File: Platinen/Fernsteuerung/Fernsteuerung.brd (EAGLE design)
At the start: 98 x 90 mm, 3 parts, among them K1 ESP32DEVKITV11000MIL, P1 TFT_3.5"_SPI_480X320, U1 COM-09032

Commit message: Eagle Fernsteuerung
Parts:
- added G1: BATT3V3_AA, HTL22_basis:BATT-3V3-AA
- moved K1 18.3 mm to (61.4, 35.2), turned to 90 degrees
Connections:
- net +3V3: now also G1.PLUS
- net GND: now also G1.MINUS, U1.B2B; no longer U1.B2A
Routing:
- net TFT_MISO: track 0.00 -> 147.3 mm
- net +3V3: track 0.00 -> 119.6 mm, vias 0 -> 2
- net TFT_CS: track 0.00 -> 91.2 mm
- net TFT_SCK: track 0.00 -> 88.2 mm
- net TFT_DC: track 0.00 -> 63.6 mm
- net TFT_RESET: track 0.00 -> 63.6 mm
- net JOYSTICK_X: track 0.00 -> 59.6 mm
- net JOYSTICK_SELECT: track 0.00 -> 27.7 mm
- net JOYSTICK_Y: track 0.00 -> 25.9 mm
- added copper zone on layer 16, net GND
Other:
- board text added: "David Kedra Diplomarbeit Fernsteuerung"

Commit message: board fersteuerung
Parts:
- added R1: 10k, HTL22_basis:R1206
- added S1: TASTERB3F-1000, HTL22_basis:B3F-10XX
- added S2: SCHALTER1SX254, HTL22_basis:SX254
- moved K1 50.4 mm to (82.1, 81.0), turned to 270 degrees
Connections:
- new net N$1: K1.4, R1.2, S1.3
- new net N$2: G1.PLUS, S2.W1
- net +3V3: now also S1.1, S2.O1; no longer G1.PLUS
- net GND: now also R1.1
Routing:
- net TFT_MISO: track 147.3 -> 0.00 mm
- net +3V3: track 119.6 -> 0.00 mm, vias 2 -> 0
- net TFT_CS: track 91.2 -> 0.00 mm
- net TFT_SCK: track 88.2 -> 0.00 mm
- net TFT_DC: track 63.6 -> 0.00 mm
- net TFT_RESET: track 63.6 -> 0.00 mm
- net JOYSTICK_X: track 59.6 -> 0.00 mm
- net JOYSTICK_SELECT: track 27.7 -> 0.00 mm
- net JOYSTICK_Y: track 25.9 -> 0.00 mm

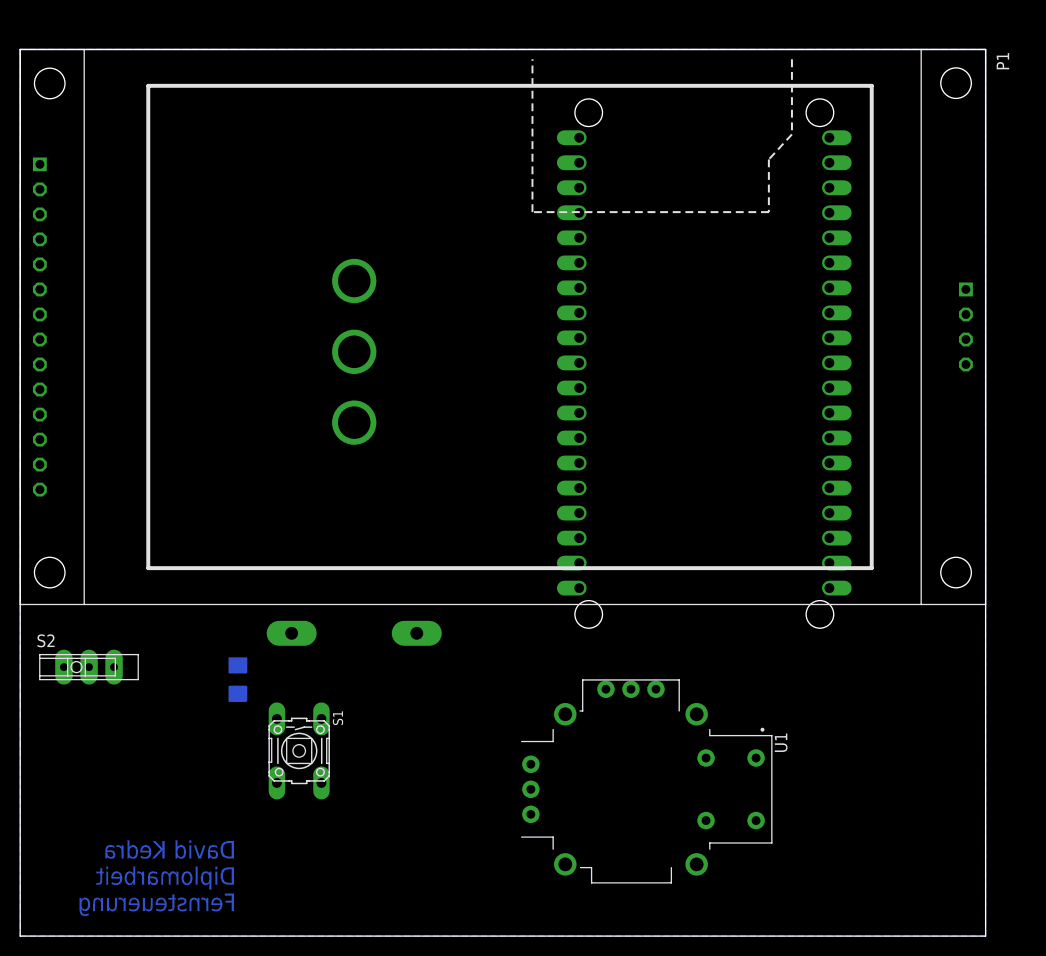
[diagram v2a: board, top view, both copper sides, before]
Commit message: Fernsteuerung Plaine fertig
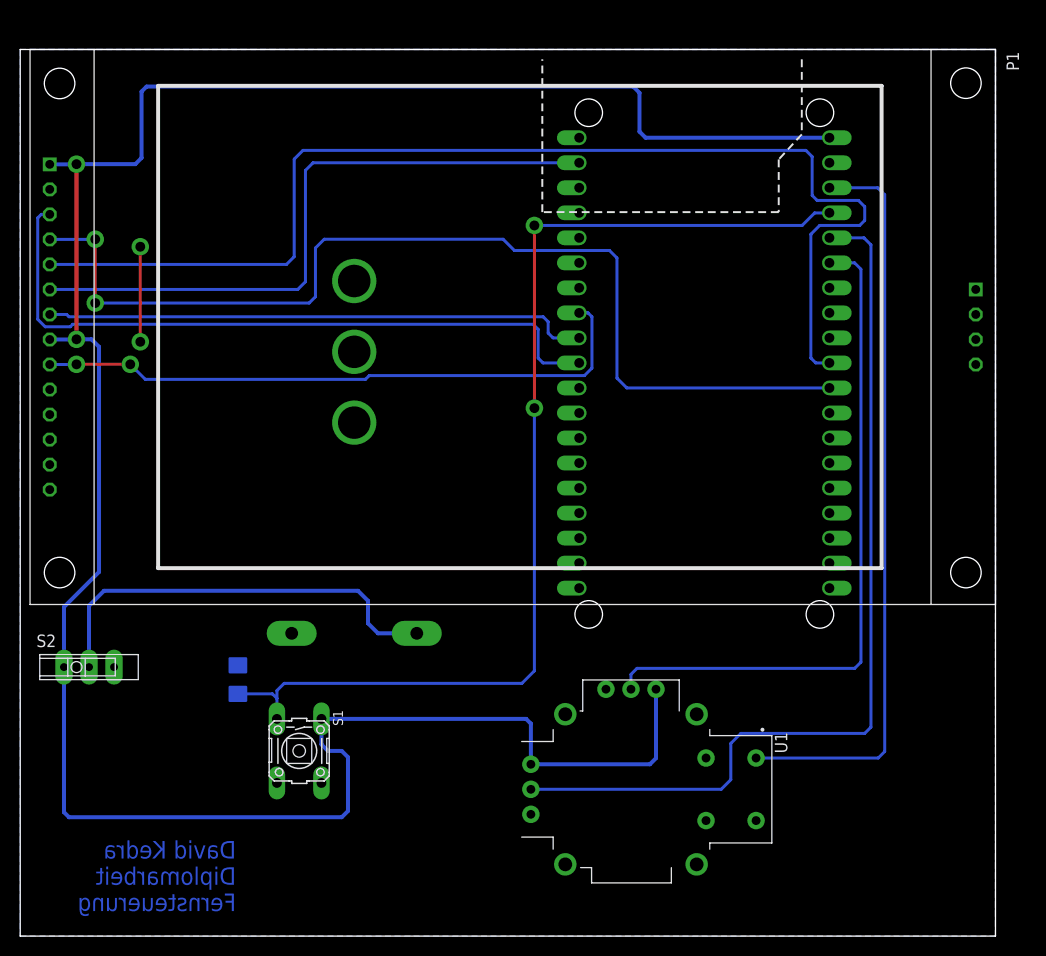
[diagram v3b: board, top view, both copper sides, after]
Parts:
- added DRILEGEND: (no value), drilegend:DRILEGEND
- moved P1 1.00 mm to (1.00, 90.0)
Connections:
- net N$1 renamed BUTTON_PULLDOWN
- net N$2 renamed BATTERY_+3V3
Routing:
- net +3V3: track 0.00 -> 249.0 mm, vias 0 -> 2
- net TFT_DC: track 0.00 -> 120.1 mm
- net BUTTON_PULLDOWN: track 0.00 -> 109.7 mm, vias 0 -> 2
- net TFT_RESET: track 0.00 -> 104.6 mm, vias 0 -> 2
- net JOYSTICK_X: track 0.00 -> 92.8 mm
- net JOYSTICK_SELECT: track 0.00 -> 75.8 mm
- net TFT_CS: track 0.00 -> 70.4 mm
- net JOYSTICK_Y: track 0.00 -> 68.7 mm
- net TFT_MOSI: track 0.00 -> 65.7 mm
- net TFT_MISO: track 0.00 -> 62.8 mm, vias 0 -> 2
- net TFT_SCK: track 0.00 -> 55.4 mm
- net BATTERY_+3V3: track 0.00 -> 43.3 mm
- net GND: track 0.00 -> 9.65 mm, vias 0 -> 2
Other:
- board size 98 x 90 mm -> 99 x 90 mm
- board text added: "01-16"
- board text added: "01-20"
- board text added: "LAYER-STACK"

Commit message: Fernsteuerung Board fertig
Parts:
- added U$1, U$2: (no value), marks:ARROW-->
- added U$3, U$4: (no value), marks:ARROW<--
- moved G1 1.00 mm to (34.9, 59.3)
- moved K1 1.00 mm to (83.1, 81.0)
- moved P1 1.00 mm to (2.00, 90.0)
- moved R1 1.00 mm to (23.1, 26.0)
- moved S1 1.00 mm to (29.3, 18.8)
- moved S2 1.00 mm to (7.99, 27.3)
- moved U1 1.00 mm to (63.0, 14.9)
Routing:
- net TFT_MISO: track 62.8 -> 64.6 mm
- net TFT_CS: track 70.4 -> 70.9 mm
- net TFT_SCK: track 55.4 -> 55.9 mm
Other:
- board size 99 x 90 mm -> 100 x 90 mm
- board text added: "100mm"
- board text added: "90mm"
- board text added: "BOTTOM"
- board text added: "TOP"
